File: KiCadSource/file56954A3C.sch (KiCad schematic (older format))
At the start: 22 parts, among them P1 USB3_TypeB, Q4 DMN6040SSD, U13 LTC4360-1

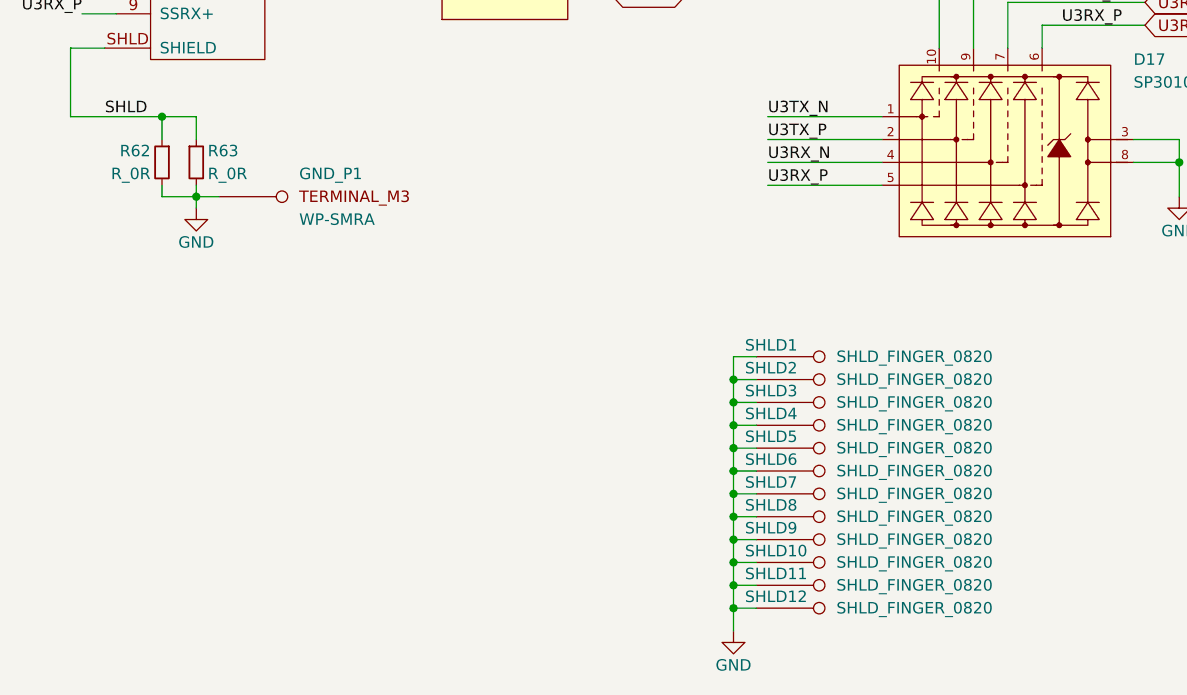
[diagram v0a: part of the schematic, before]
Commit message: first production run, digital GPIOs, replaced parts (see CHANGES.txt)
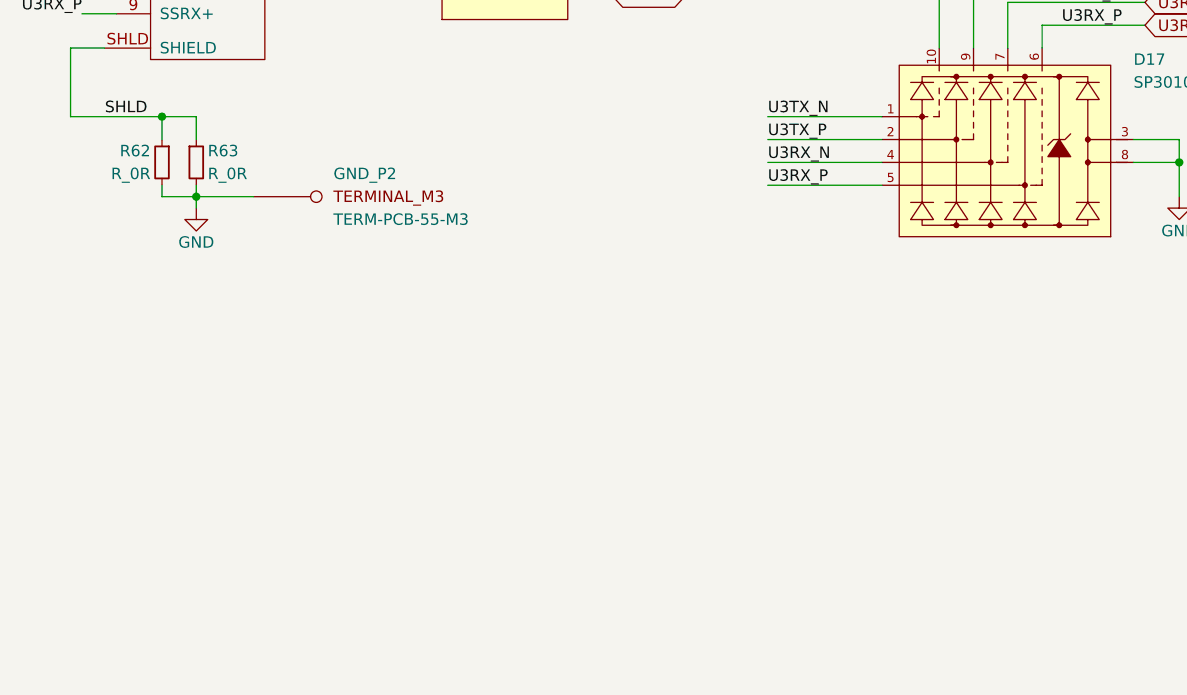
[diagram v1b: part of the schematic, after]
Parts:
- removed GND_P1: WP-SMRA, ScopefunPackagesLibrary:WP-SMRA, symbol WP-SMRA
- removed SHLD1, SHLD10, SHLD11, SHLD12, SHLD2, SHLD3, SHLD4, SHLD5, SHLD6, SHLD7, SHLD8, SHLD9: SHLD_FINGER_0820, ScopefunPackagesLibrary:EMI_SHLD_FINGER_0820, symbol SHLD_FINGER_0820
- added GND_P2: TERM-PCB-55-M3, ScopefunPackagesLibrary:TERM-PCB-55-M3, symbol TERM-PCB-55-M3
- C70: Description MLCC - SMD/SMT 0603 6.3V X5R 20% -> MLCC - SMD/SMT 0603 6.3V X5R 10%
- R62, R63: Description RES SMD 1% 1/10W 0805 -> RES SMD ZERO OHM JUMPER 0805
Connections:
- net GND: now also GND_P2.1
